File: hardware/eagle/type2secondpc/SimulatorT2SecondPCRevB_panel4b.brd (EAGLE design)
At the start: 99.1 x 99.1 mm, 37 parts

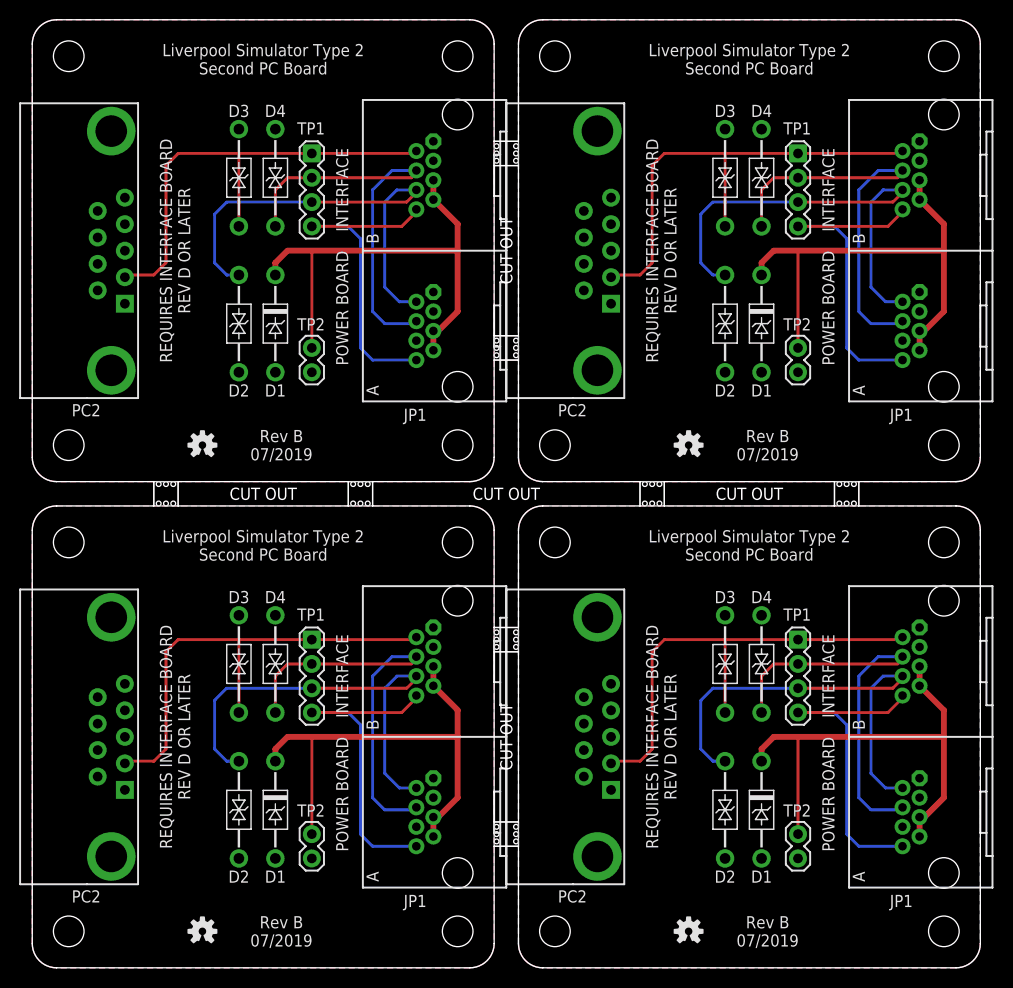
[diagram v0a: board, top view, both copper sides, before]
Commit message: Wider 5mm break-offs
Issues with JLPCB rejecting panelised boards with 2.5mm stamp hole
break-off tabs. Increased tab width to 5mm on all panelised boards.
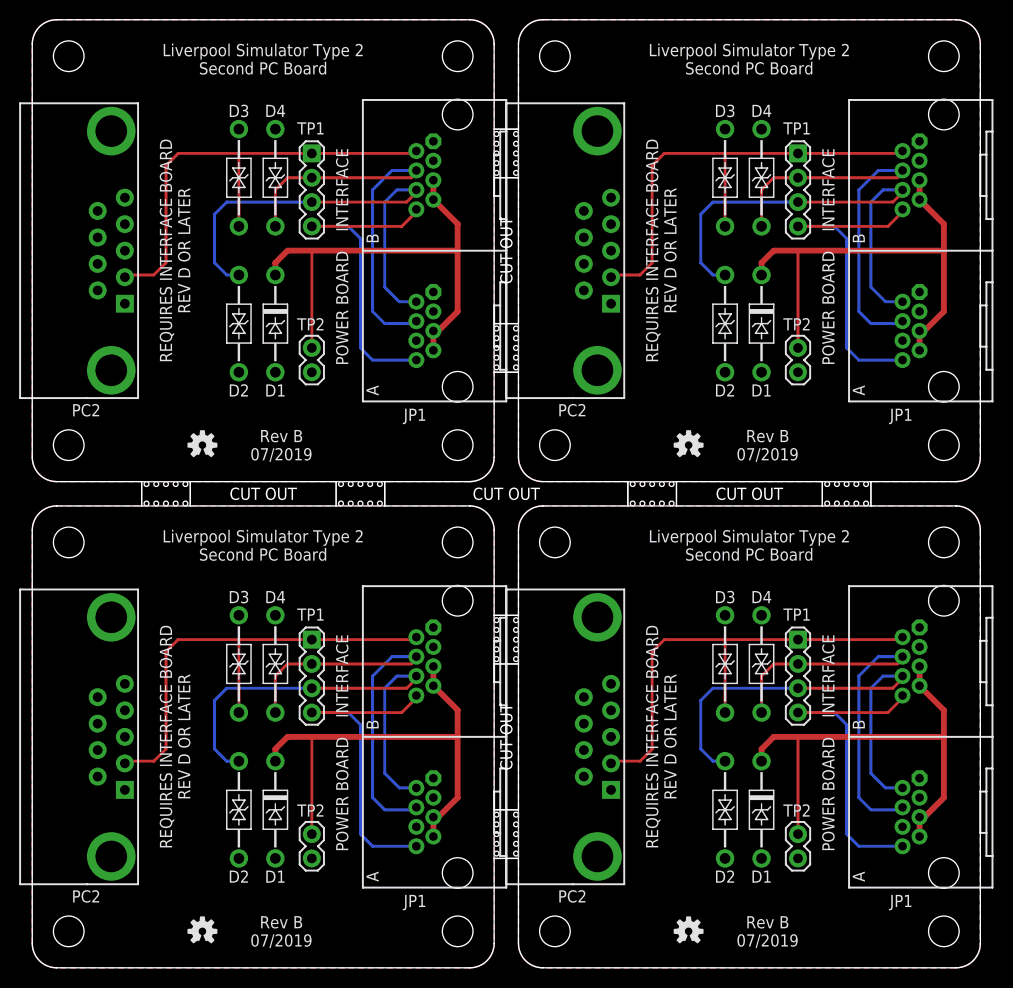
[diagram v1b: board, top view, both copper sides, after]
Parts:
- E$1: device AIC_Custom:OUTLINE_PANEL_4 -> AIC_Custom:OUTLINE_PANEL_4_5MM
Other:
- outline, holes or cut-outs redrawn
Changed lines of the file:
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@@
 <attribute name="NAME1" value="D1" x="76.2" y="60.96" size="1.27" layer="25" font="vector" rot="R180" align="bottom-center"/>
 </element>
-<element name="E$1" library="AIC_Custom" package="OUTLINE_PANEL_4" value="" x="0" y="0"/>
+<element name="E$1" library="AIC_Custom" package="OUTLINE_PANEL_4_5MM" value="" x="0" y="0"/>
 </elements>
 <signals>
